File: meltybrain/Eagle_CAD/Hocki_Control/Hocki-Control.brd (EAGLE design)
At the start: 90 x 46 mm, 150 parts, among them J1 SM03B-SRSS-TB(LF)(SN), J2 SM03B-SRSS-TB(LF)(SN), J3 SM03B-SRSS-TB(LF)(SN), J4 SM04B-SRSS-TB(LF)(SN), J5 SM04B-SRSS-TB(LF)(SN), J6 SM02B-SRSS-TB(LF)(SN), U1 TEENSY_4.1, U10 TLV3502AIDCNR, U11 NL27WZ32USG, U12 NL27WZ32USG, U13 HMC1052L-TR, U14 LMV358, U15 IRF7509, U16 TMUX1219DCKR, U17 LMV358, U18 LMV358, U19 AP2210K-3.3TRG1, U2 ADXL375, U20 AP2210K-5.0TRG1, U21 AP63200, U22 74AHC1G04GW,125, U23 LDL212PU50R, U3 ADXL375, U4 ADXL375, U5 ADXL375, U6 LMH6612MAX/NOPB, U7 LMH6612MAX/NOPB, U8 LMH6612MAX/NOPB, U9 LMH6612MAX/NOPB

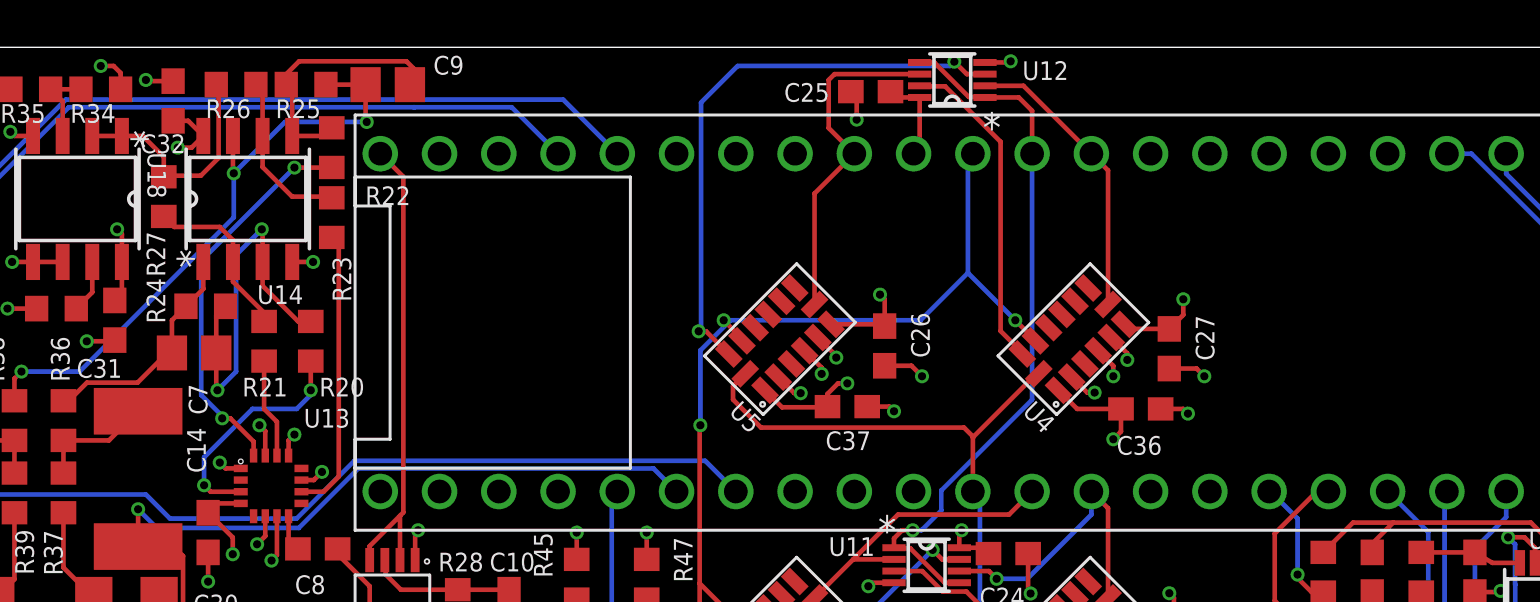
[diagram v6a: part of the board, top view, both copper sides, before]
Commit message: temperature sensor
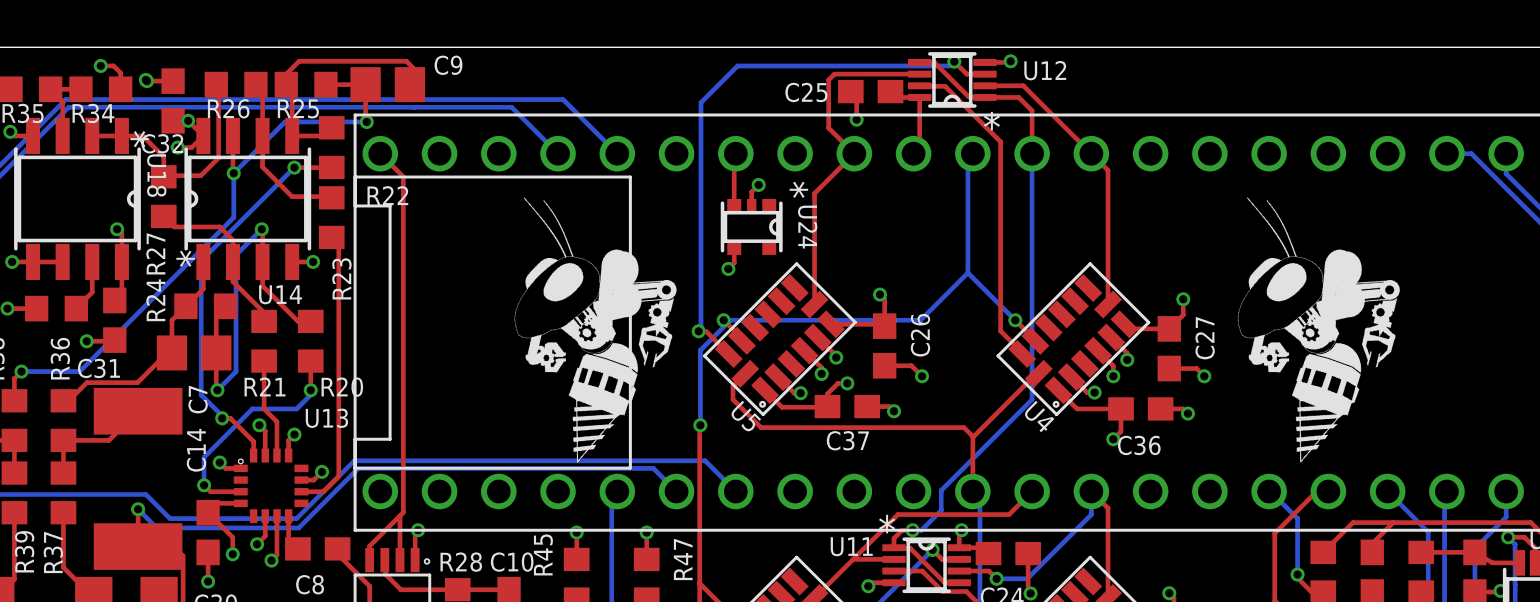
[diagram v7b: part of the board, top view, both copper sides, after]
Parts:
- added U$1, U$2: (no value), RoboJackets-Aesthetics:ROBOBUZZ_0.6X
- added U24: TMP235A4DCKR, Hocki_Library:SOT-353
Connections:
- new net TEMP: U1.26, U24.3
- net 3.3V: now also U24.4
- net GND: now also U24.2
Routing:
- net TEMP: track 0.00 -> 2.27 mm
- net GND: track 122.3 -> 123.3 mm, vias 100 -> 102
- net 3.3V: track 54.1 -> 55.1 mm, vias 13 -> 14
- net +3V3: vias 10 -> 11
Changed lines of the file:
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@@
 <drawing>
 <settings>
-<setting alwaysvectorfont="no"/>
+<setting alwaysvectorfont="yes"/>
 <setting verticaltext="up"/>
 </settings>
@@
 <layers>
 <layer number="1" name="Top" color="4" fill="1" visible="yes" active="yes"/>
-<layer number="2" name="GND" color="16" fill="1" visible="yes" active="yes"/>
+<layer number="2" name="GND" color="56" fill="1" visible="yes" active="yes"/>
 <layer number="3" name="Route3" color="17" fill="1" visible="no" active="no"/>
 <layer number="4" name="Route4" color="18" fill="1" visible="no" active="no"/>
@@
 <layer number="13" name="Route13" color="21" fill="1" visible="no" active="no"/>
 <layer number="14" name="Route14" color="22" fill="1" visible="no" active="no"/>
-<layer number="15" name="Power" color="23" fill="1" visible="yes" active="yes"/>
-<layer number="16" name="Bottom" color="1" fill="1" visible="yes" active="yes"/>
+<layer number="15" name="Power" color="22" fill="1" visible="yes" active="yes"/>
+<layer number="16" name="Bottom" color="9" fill="1" visible="yes" active="yes"/>
 <layer number="17" name="Pads" color="2" fill="1" visible="yes" active="yes"/>
 <layer number="18" name="Vias" color="2" fill="1" visible="yes" active="yes"/>
@@
 <attribute name="VALUE" x="23.6" y="1.8" size="1" layer="27" font="vector" align="top-left"/>
 </element>
+<element name="U$1" library="RoboJackets-Aesthetics" package="ROBOBUZZ_0.6X" value="" x="11" y="1" smashed="yes"/>
+<element name="U$2" library="RoboJackets-Aesthetics" package="ROBOBUZZ_0.6X" value="" x="-20" y="1" smashed="yes"/>
+<element name="U24" library="Hocki_Library" package="SOT-353" value="TMP235A4DCKR" x="-12.5" y="11.1" smashed="yes" rot="R270">
+<attribute name="NAME" x="-10.5" y="12.1" size="0.8" layer="25" font="vector" ratio="15" rot="SR270"/>
+<attribute name="VALUE" x="-14.5" y="12.1" size="1" layer="27" font="vector" rot="SR270" align="top-left"/>
+</element>
 </elements>
 <signals>
@@
 <wire x1="-25.4052" y1="-20" x2="-25" y2="-20.4052" width="0.2" layer="1"/>
 <via x="-25" y="-20.4052" extent="1-16" drill="0.35"/>
+<contactref element="U24" pad="2"/>
+<wire x1="-12.5" y1="12" x2="-12.5" y2="12.6" width="0.2" layer="1"/>
+<wire x1="-12.5" y1="12.6" x2="-12.2" y2="12.9" width="0.2" layer="1"/>
+<via x="-12.2" y="12.9" extent="1-16" drill="0.35"/>
+<via x="-38.4186" y="17.35" extent="1-16" drill="0.35"/>
 </signal>
 <signal name="3.3V">
@@
 <contactref element="D17" pad="C2"/>
 <wire x1="25.15" y1="2" x2="24.2" y2="2" width="0.2" layer="1"/>
+<contactref element="U24" pad="4"/>
+<wire x1="-13.25" y1="10.2" x2="-13.25" y2="9.55" width="0.2" layer="1"/>
+<wire x1="-13.25" y1="9.55" x2="-13.5" y2="9.3" width="0.2" layer="1"/>
+<via x="-13.5" y="9.3" extent="1-16" drill="0.35"/>
 </signal>
 <signal name="MOSI">
@@
 <wire x1="-31.5" y1="-9.2" x2="-31.5" y2="-8.3" width="0.2" layer="1"/>
 <wire x1="-31.5" y1="-8.3" x2="-31.2" y2="-8" width="0.2" layer="1"/>
+<via x="-36.655" y="15.65" extent="1-16" drill="0.35"/>
 </signal>
 <signal name="9V">
@@
 <wire x1="-51" y1="-17.15" x2="-51" y2="-15.85" width="0.2" layer="1"/>
 </signal>
+<signal name="TEMP">
+<contactref element="U24" pad="3"/>
+<contactref element="U1" pad="26"/>
+<wire x1="-13.25" y1="12" x2="-13.25" y2="14.17" width="0.2" layer="1"/>
+<wire x1="-13.25" y1="14.17" x2="-13.18" y2="14.24" width="0.2" layer="1"/>
+</signal>
 </signals>
 <mfgpreviewcolors>
-<mfgpreviewcolor name="soldermaskcolor" color="0xC8008000"/>
+<mfgpreviewcolor name="soldermaskcolor" color="0xC8000000"/>
 <mfgpreviewcolor name="silkscreencolor" color="0xFFFEFEFE"/>
 <mfgpreviewcolor name="backgroundcolor" color="0xFF282828"/>

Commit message: done
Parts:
- added C55: 1uF, rcl:C0603
- C1, C2, C3, C46: value 47nF -> 0.1uF; device rcl:C1206 -> rcl:C0603
- C11: value 1uF -> 2.2uF
- C13: value 47nF -> 2.2uF; device rcl:C1206 -> rcl:C0603
- C14: value 0.18uF -> 100pF; device Hocki_Library:ECH-U1H184GX9 -> rcl:C0603
- C15: value 47nF -> 100pF; device rcl:C1206 -> rcl:C0603
- C16: value 0.18uF -> 0.1u; device Hocki_Library:ECH-U1H184GX9 -> rcl:C0603
- C17: value 0.1uF -> 1uF
- C18: value 0.1uF -> 4.7uF
- C22, C23, C24, C25, C29, C31, C50: value 0.1uF -> 47nF; device rcl:C0603 -> rcl:C1206
- C30, C32: value 0.1uF -> 62nF; device rcl:C0603 -> Hocki_Library:BFC241646203
- C39, C41: value 1uF -> 0.1uF
- C4: value 47nF -> 10uF
- C40: value 2.2uF -> 0.1uF
- C42, C43, C49: value 100pF -> 0.1uF
- C44: value 2.2uF -> 1000pF; device rcl:C0603 -> rcl:C0805
- C45: value 47nF -> 0.18uF; device rcl:C1206 -> Hocki_Library:ECH-U1H184GX9
- C47: value 10uF -> 0.1uF; device rcl:C1206 -> rcl:C0603
- C48: value 22uF -> 47nF
- C5: value 62nF -> 100pF; device Hocki_Library:BFC241646203 -> rcl:C0603
- C51: value 0.1u -> 0.18uF; device rcl:C0603 -> Hocki_Library:ECH-U1H184GX9
- C52: value 22uF -> 1000pF; device rcl:C1206 -> rcl:C0805
- C53: value 4.7uF -> 0.1uF
- C54: value 1uF -> .1uF
- C6: value 62nF -> 22uF; device Hocki_Library:BFC241646203 -> rcl:C1206
- C7: value 1000pF -> 22uF; device rcl:C0805 -> rcl:C1206
- C8: value .1uF -> 1uF
- C9: value 1000pF -> 1uF; device rcl:C0805 -> rcl:C0603
- D1: value RB521S30T1G -> PESD4V0Y1BSFYL; device Hocki_Library:SOD-523 -> Hocki_Library:DSN0603-2
- D10, D9: value GREEN -> BAS581-02V-V-G-08; device SparkFun-LED:LED-0603 -> Hocki_Library:SOD-523
- D12: value GREEN -> PESD5V0H1BSFYL; device SparkFun-LED:LED-0603 -> Hocki_Library:DSN0603-2
- D13: value GREEN -> PESD4V0Y1BSFYL; device SparkFun-LED:LED-0603 -> Hocki_Library:DSN0603-2
- D14: value ESDZX051-1BF4 -> GREEN; device Hocki_Library:DSN0603-2 -> SparkFun-LED:LED-0603
- D15: value PESD5V0H1BSFYL -> BAS581-02V-V-G-08; device Hocki_Library:DSN0603-2 -> Hocki_Library:SOD-523
- D16, D17: value PESD4V0Y1BSFYL -> RB521S30T1G; device Hocki_Library:DSN0603-2 -> Hocki_Library:SOD-523
- D2: value RB521S30T1G -> BAS581-02V-V-G-08
- D3: value D26V0H1U2LP20-7 -> GREEN; device Hocki_Library:D26V0H1U2LP20-7 -> SparkFun-LED:LED-0603
- D4: value BAS581-02V-V-G-08 -> D26V0H1U2LP20-7; device Hocki_Library:SOD-523 -> Hocki_Library:D26V0H1U2LP20-7
- D5, D7: value BAS581-02V-V-G-08 -> GREEN; device Hocki_Library:SOD-523 -> SparkFun-LED:LED-0603
- D6: value BAS581-02V-V-G-08 -> ESDZX051-1BF4; device Hocki_Library:SOD-523 -> Hocki_Library:DSN0603-2
- J2: value SM03B-SRSS-TB(LF)(SN) -> SM04B-SRSS-TB(LF)(SN); device Hocki_Library:SM03B-SRSS-TB(LF)(SN) -> Hocki_Library:SM04B-SRSS-TB(LF)(SN)
- J3: value SM03B-SRSS-TB(LF)(SN) -> SM02B-SRSS-TB(LF)(SN); device Hocki_Library:SM03B-SRSS-TB(LF)(SN) -> Hocki_Library:SM02B-SRSS-TB(LF)(SN)
- J5: value SM04B-SRSS-TB(LF)(SN) -> SM03B-SRSS-TB(LF)(SN); device Hocki_Library:SM04B-SRSS-TB(LF)(SN) -> Hocki_Library:SM03B-SRSS-TB(LF)(SN)
- J6: value SM02B-SRSS-TB(LF)(SN) -> SM03B-SRSS-TB(LF)(SN); device Hocki_Library:SM02B-SRSS-TB(LF)(SN) -> Hocki_Library:SM03B-SRSS-TB(LF)(SN)
- R1: value 205k -> 665
- R10, R11: value 4.5k -> 169
- R13: value 169 -> 665
- R14, R45, R47: value 169 -> 499
- R15: value 20k -> 330
- R16: value 44.2k -> 4.5k
- R17: value 44.2k -> 169
- R18: value 30 -> 169
- R19: value 30 -> 4.5k
- R2: value 499 -> 665
- R20, R21, R31: value 4.99k -> 169
- R22, R32: value 4.99k -> 10k
- R23: value 4.99k -> 30
- R24: value 499k -> 44.2k
- R25: value 499k -> 30
- R26: value 499k -> 4.5k
- R27: value 499k -> 169
- R28: value 200 -> 169
- R29: value 665 -> 4.5k
- R3: value 169 -> 205k
- R30: value 330 -> 44.2k
- R33, R42: value 499 -> 499k
- R34: value 499 -> 40.2k
- R35: value 499 -> 7.32k
- R36, R38: value 40.2k -> 4.99k
- R37: value 7.32k -> 4.99k
- R39: value 7.32k -> 40.2k
- R4: value 4.5k -> 499
- R40: value 10k -> 7.32k
- R41: value 10k -> 4.99k
- R43: value 665 -> 499k
- R44: value 330 -> 499k
- R46: value 330 -> 200
- R48: value 665 -> 499
- R5: value 4.5k -> 20k
- R6, R8: value 169 -> 330
- R7, R9: value 169 -> 4.99k
- U1: value TEENSY_4.1 -> AP63200; device Hocki_Library:TEENSY_4.1 -> Hocki_Library:SOT-23-6
- U10: value TLV3502AIDCNR -> LMH6612MAX/NOPB; device Hocki_Library:SOT-23-8 -> Hocki_Library:8-SOIC
- U11: value NL27WZ32USG -> TLV3502AIDCNR; device Hocki_Library:US8 -> Hocki_Library:SOT-23-8
- U12: value NL27WZ32USG -> LMH6612MAX/NOPB; device Hocki_Library:US8 -> Hocki_Library:8-SOIC
- U13: value HMC1052L-TR -> TMP235A4DCKR; device Hocki_Library:16-LCC -> Hocki_Library:SOT-353
- U14, U17: value LMV358 -> ADXL375; device Hocki_Library:8-SOIC -> Hocki_Library:14-LGA
- U15: value IRF7509 -> NL27WZ32USG; device Hocki_Library:MICRO8 -> Hocki_Library:US8
- U16: value TMUX1219DCKR -> ADXL375; device Hocki_Library:SOT-363 -> Hocki_Library:14-LGA
- U18: value LMV358 -> NL27WZ32USG; device Hocki_Library:8-SOIC -> Hocki_Library:US8
- U19: value AP2210K-3.3TRG1 -> ADXL375; device Hocki_Library:SOT-23-5 -> Hocki_Library:14-LGA
- U2: value ADXL375 -> TEENSY_4.1; device Hocki_Library:14-LGA -> Hocki_Library:TEENSY_4.1
- U20: value AP2210K-5.0TRG1 -> LMV358; device Hocki_Library:SOT-23-5 -> Hocki_Library:8-SOIC
- U21: value AP63200 -> LMV358; device Hocki_Library:SOT-23-6 -> Hocki_Library:8-SOIC
- U22: value 74AHC1G04GW,125 -> HMC1052L-TR; device Hocki_Library:SOT-353 -> Hocki_Library:16-LCC
- U23: value LDL212PU50R -> LMV358; device Hocki_Library:DFN6(3X3) -> Hocki_Library:8-SOIC
- U24: value TMP235A4DCKR -> IRF7509; device Hocki_Library:SOT-353 -> Hocki_Library:MICRO8
- U3: value ADXL375 -> AP2210K-5.0TRG1; device Hocki_Library:14-LGA -> Hocki_Library:SOT-23-5
- U4: value ADXL375 -> AP2210K-3.3TRG1; device Hocki_Library:14-LGA -> Hocki_Library:SOT-23-5
- U5: value ADXL375 -> 74AHC1G04GW,125; device Hocki_Library:14-LGA -> Hocki_Library:SOT-353
- U6: value LMH6612MAX/NOPB -> LDL212PU50R; device Hocki_Library:8-SOIC -> Hocki_Library:DFN6(3X3)
- U9: value LMH6612MAX/NOPB -> TMUX1219DCKR; device Hocki_Library:8-SOIC -> Hocki_Library:SOT-363
- moved D8 85.5 mm to (36.1, -12.0), turned to 270 degrees
- moved U23 80.8 mm to (-41.7, 12.3)
- moved J3 80.1 mm to (-47.0, 10.0), turned to 270 degrees
- moved C53 77.0 mm to (-41.1, 7.60), flipped to the bottom
- moved C51 72.7 mm to (-48.4, 0.30)
- moved C16 71.7 mm to (23.5, 11.1)
- moved R40 70.1 mm to (-45.1, -0.30), turned to 90 degrees
- moved C32 69.8 mm to (26.5, -11.7), turned to 0 degrees
- moved C54 66.9 mm to (-31.1, -3.50), turned to 90 degrees
- moved C30 64.8 mm to (26.5, -19.9), turned to 0 degrees
- moved R24 64.2 mm to (21.4, -21.2), turned to 90 degrees
- moved D15 63.3 mm to (37.3, -15.2), turned to 90 degrees
- moved C5 63.0 mm to (-39.1, -13.1), turned to 180 degrees
- moved D12 62.4 mm to (-25.8, -20.0), turned to 180 degrees
- moved J2 61.6 mm to (33.0, 0.00), turned to 90 degrees
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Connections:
- net +24V: now also C4.1, D2.1, R1.2, U1.2, U1.3; no longer C47.1, D3.1, R48.2, U21.2, U21.3
- net +3V3: now also C13.1, C46.1, C47.1, C49.1, C53.1, D10.2, D13.C2, R10.2, R45.1, R46.1, U20.8, U21.8, U22.4, U23.8, U4.5; no longer C30.1, C31.1, C32.1, C33.1, C40.1, D16.C2, D6.2, R28.1, R34.1, R45.2, U13.4, U14.8, U17.8, U18.8, U19.5
- net +5V: now also C18.1, D15.2, J2.1, J2.S1, J2.S2, R8.2, U6.2, U6.3; no longer C53.1, D7.2, J5.1, J5.S1, J5.S2, R46.2, U23.2, U23.3
- net 1.66V_REF_BUF: now also C24.2, C25.2, C31.2, R19.1, R20.1, R29.1, R31.1, U8.6, U8.7; no longer C1.2, C3.2, C45.2, R10.1, R13.1, R4.1, R7.1, U6.6, U6.7
- net 1.6V_REF: now also R13.1, R15.2, U8.5; no longer R29.1, R30.2, U6.5
- net 10K_FB: now also C22.2, C23.2, R17.2; no longer C2.2, C46.2, R3.2
- net 10K_IN: now also C24.1, C25.1, R16.1, R17.1, R19.2; no longer C1.1, C45.1, R3.1, R4.2, R5.1
- net 10K_INT: now also R22.1, U11.7, U2.23; no longer R40.1, U1.23, U10.7
- net 10K_OUT: now also R12.2, R18.1, U12.3; no longer R6.2, R8.1, U9.3
- net 10K_PEAK: now also C30.1, D16.1, R23.2, R24.2, U12.2, U2.20; no longer C5.1, D1.1, R17.2, R18.2, U1.20, U9.2
- net 10K_REF: now also C8.1, R7.2, U11.2; no longer C12.1, R31.2, U10.2
- net 20K_FB: now also C29.2, R27.2, U10.7; no longer C4.2, R9.2, U8.7
- net 20K_IN: now also C31.1, R26.1, R27.1, R29.2, U10.3; no longer C3.1, R10.2, R11.1, R9.1, U8.3
- net 20K_INT: now also R32.1, U11.6, U2.22; no longer R41.1, U1.22, U10.6
- net 20K_OUT: now also R21.2, R28.1, U10.1, U12.5; no longer R12.2, R14.1, U8.1, U9.5
- net 20K_PEAK: now also C32.1, D17.1, R25.2, R30.2, U12.6, U2.21; no longer C6.1, D2.1, R16.2, R19.2, U1.21, U9.6
- net 20K_REF: now also C9.1, R9.2, U11.4; no longer C11.1, R32.2, U10.4
- net 3.3V: now also C1.1, C16.1, C33.1, C39.1, C40.1, C41.1, C42.1, C43.1, D1.C2, R11.2, U13.4, U14.1, U14.6, U15.8, U16.1, U16.6, U17.1, U17.6, U18.8, U19.1, U19.6, U2.3.3V1, U2.3.3V2, U5.5; no longer C22.1, C23.1, C24.1, C25.1, C26.1, C29.1, C51.1, D17.C2, R47.2, U1.3.3V1, U1.3.3V2, U10.8, U2.1, U2.6, U22.5, U24.4, U3.1, U3.6, U4.1, U4.6, U5.1, U5.6, U9.8
- net 5V: now also C11.1, C12.1, C2.1, C26.1, D10.1, D12.C2, D9.2, J1.2, J1.S1, J1.S2, R13.2, R6.2, U10.8, U2.5V, U3.5, U4.1, U4.3, U9.2; no longer C17.1, C18.1, C39.1, C44.1, D15.C2, D5.2, D6.1, J3.2, J3.S1, J3.S2, R29.2, R44.2, U1.5V, U16.2, U19.1, U19.3, U20.5, U6.8
- net 9V: now also C10.1, C17.1, C5.1, C6.1, C7.1, D15.1, D2.2, D6.C2, D9.1, J5.1, J6.1, R3.1, R4.2, U3.1, U3.3, U6.4, U6.6; no longer C41.1, C48.1, C49.1, C52.1, C54.1, D14.C2, D4.2, D5.1, D7.1, J1.1, J2.1, R1.1, R42.2, U20.1, U20.3, U23.4, U23.6
- net CS1: now also U14.7, U15.2, U2.14; no longer U1.14, U11.2, U2.7
- net CS2: now also U15.6, U16.7, U2.15; no longer U1.15, U11.6, U3.7
- net CS3: now also U17.7, U18.2, U2.10; no longer U1.10, U12.2, U4.7
- net CS4: now also U18.6, U19.7, U2.24; no longer U1.24, U12.6, U5.7
- net ESC_L: now also J3.1, U2.28; no longer J6.1, U1.28
- net ESC_R: now also J3.2, U2.29; no longer J6.2, U1.29
- net GND: now also C1.2, C14.2, C16.2, C2.2, C4.2, C46.2, C49.2, C50.2, C55.2, C7.2, C8.2, C9.2, D1.C1, D12.C1, D13.C1, D14.C, D3.C, D4.2, D5.C, D6.C1, D7.C, J2.4, J3.S1, J3.S2, J5.3, J5.S1, J5.S2, J6.3, R14.1, R15.1, R24.1, R47.2, R48.2, R5.2, U1.4, U10.4, U11.5, U13.2, U14.2, U14.5, U15.4, U16.2, U16.4, U16.5, U17.2, U17.5, U19.4, U19.5, U2.GND1, U2.GND2, U2.GND3, U20.4, U22.1, U22.11, U22.13, U22.15, U22.6, U22.7, U23.4, U23.5, U23.6, U24.1, U5.3, U6.1, U6.7, U9.3; no longer C22.2, C23.2, C24.2, C25.2, C29.2, C31.2, C44.2, C5.2, C51.2, C52.2, C54.2, D10.C, D12.C, D13.C, D14.C1, D15.C1, D16.C1, D17.C1, D3.2, D9.C, J1.S1, J1.S2, J2.3, J2.S1, J2.S2, J3.3, J5.4, R15.2, R16.1, R17.1, R2.1, R33.2, R35.2, U1.GND1, U1.GND2, U1.GND3, U10.5, U11.4, U13.1, U13.11, U13.13, U13.15, U13.6, U13.7, U15.1, U16.3, U18.5, U18.6, U2.2, U2.4, U2.5, U20.2, U22.3, U23.1, U23.7, U24.2, U3.4, U3.5, U4.4, U4.5, U5.2, U5.4, U5.5, U6.4, U9.4
- net IR_BOTTOM: now also J6.2, U9.6; no longer J2.2, U16.6
- net IR_SEL: now also U2.37, U9.1; no longer U1.37, U16.1
- net IR_TOP: now also J5.2, U9.4; no longer J1.2, U16.4
- net LED_CLK1: now also J2.2, U2.2; no longer J4.2, U1.2
- net LED_CLK2: now also J4.2, U2.4; no longer J5.2, U1.4
- net LED_DATA1: now also J2.3, U2.1; no longer J4.3, U1.1
- net LED_DATA2: now also J4.3, U2.3; no longer J5.3, U1.3
- net MAG_FILT_A: now also C45.2, U2.38, U21.1, U21.2; no longer C14.2, U1.38, U17.1, U17.2
- net MAG_FILT_B: now also C51.2, U2.39, U21.6, U21.7; no longer C16.2, U1.39, U17.6, U17.7
- net MAG_OUTPUTA: now also C44.2, R33.1, R34.2, U20.1; no longer C7.2, R24.1, R36.2, U14.1
- net MAG_OUTPUTB: now also C52.2, R39.2, R44.1, U20.7; no longer C9.2, R25.1, R38.2, U14.7
- net MISO: now also U14.12, U16.12, U17.12, U19.12; no longer U1.12, U3.12, U4.12, U5.12
- net MOSI: now also U15.1, U15.5, U18.1, U18.5, U2.11; no longer U1.11, U11.1, U11.5, U12.1, U12.5
- net MOSI1: now also U14.13, U15.7; no longer U11.7, U2.13
- net MOSI2: now also U15.3, U16.13; no longer U11.3, U3.13
- net MOSI3: now also U17.13, U18.7; no longer U12.7, U4.13
- net MOSI4: now also U18.3, U19.13; no longer U12.3, U5.13
- net N$1: now also C3.1, U1.6; no longer C50.1, U21.6
- net N$10: now also C29.1, R21.1, U10.2, U10.6; no longer C4.1, R12.1, U8.2, U8.6
- net N$11: now also C15.1, U4.4; no longer C43.1, U19.4
- net N$12: now also C5.2, R3.2, R5.1, U1.1; no longer C49.2, R1.2, R15.1, U21.1
- net N$13: now also R28.2, R31.2, U10.5; no longer R13.2, R14.2, U8.5
- net N$14: now also D8.A, R8.1; no longer D12.A, R46.1
- net N$15: now also D7.A, R6.1; no longer D10.A, R44.1
- net N$16: now also C54.1, U24.5, U24.6, U24.7, U24.8; no longer C8.1, U15.5, U15.6, U15.7, U15.8
- net N$17: now also R10.1; no longer R45.1
- net N$18: now also D5.A, R4.1; no longer D9.A, R42.1
- net N$19: now also D3.A, R2.1; no longer D8.A, R43.1
- net N$2: now also D16.2, U12.1; no longer D1.2, U9.1
- net N$20: now also R1.1, R2.2; no longer R43.2, R48.1
- net N$21: now also R7.1, U2.18; no longer R31.1, U1.18
- net N$22: now also R9.1, U2.19; no longer R32.1, U1.19
- net N$23: now also R45.2, R47.1, U23.3; no longer R34.2, R35.1, U18.3
- net N$24: now also R48.1, U23.7; no longer R33.1, U18.7
- net N$25: now also C45.1, R34.1, R35.2; no longer C14.1, R36.1, R37.2
- net N$26: now also C48.1, R35.1, U21.3; no longer C13.1, R37.1, U17.3
- net N$27: now also D14.A, R11.1; no longer D13.A, R47.1
- net N$29: now also C51.1, R39.1, R40.2; no longer C16.1, R38.1, R39.2
- net N$3: now also C3.2, U1.5; no longer C50.2, U21.5
- net N$30: now also C50.1, R40.1, U21.5; no longer C15.1, R39.1, U17.5
- net N$34: now also R41.1, R43.1, U20.6; no longer R23.1, R26.1, U14.6
- net N$35: now also C52.1, R38.1, R44.2, U20.5; no longer C9.1, R22.1, R25.2, U14.5
- net N$36: now also R37.1, R42.1, U20.2; no longer R21.1, R27.1, U14.2
- net N$37: now also C44.1, R33.2, R36.1, U20.3; no longer C7.1, R20.1, R24.2, U14.3
- net N$4: now also C22.1, C23.1, R12.1; no longer C2.1, C46.1, R6.1
- net N$5: now also R22.2, R23.1, U11.1; no longer R18.1, R40.2, U10.1
- net N$6: now also R25.1, R32.2, U11.3; no longer R19.1, R41.2, U10.3
- net N$7: now also R18.2, R20.2; no longer R7.2, R8.2
- net N$8: now also C14.1, U3.4; no longer C42.1, U20.4
- net N$9: now also D17.2, U12.7; no longer D2.2, U9.7
- net OUT+(A): now also R36.2, U22.3; no longer R20.2, U13.3
- net OUT+(B): now also R38.2, U22.16; no longer R22.2, U13.16
- net OUT-(A): now also R37.2, U22.14; no longer R21.2, U13.14
- net OUT-(B): now also R41.2, U22.10; no longer R23.2, U13.10
- net RC_SIGNAL: now also J1.1, U5.2; no longer J3.1, U22.2
- net S/R: now also U2.32, U24.2, U24.4; no longer U1.32, U15.2, U15.4
- net S/R+: now also C54.2, U22.8; no longer C8.2, U13.8
- net SBUS: now also U2.0, U5.4; no longer U1.0, U22.4
- net SCLK: now also U14.14, U16.14, U17.14, U19.14, U2.13; no longer U1.13, U2.14, U3.14, U4.14, U5.14
- net TEMP: now also U13.3, U2.26; no longer U1.26, U24.3
- net VG_SIGNAL: now also R14.2, U8.3, U9.5; no longer R2.2, U16.5, U6.3
- net VG_SIGNAL_BUF: now also R16.2, R26.2, U8.1, U8.2; no longer R11.2, R5.2, U6.1, U6.2
- net VREF/2: now also R42.2, R43.2, U23.1, U23.2; no longer R26.2, R27.2, U18.1, U18.2
- net VSR: now also C55.1, R46.2, U24.3; no longer C10.1, R28.2, U15.3
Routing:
- net N$24: track 2.28 -> 7.14 mm, vias 0 -> 1
- net 1.6V_REF: track 15.1 -> 10.4 mm, vias 0 -> 1
- net N$4: track 19.4 -> 14.8 mm
- net 3.3V: track 55.1 -> 50.4 mm, vias 14 -> 15
- net N$23: track 3.51 -> 6.22 mm, vias 0 -> 1
- net GND: track 123.3 -> 120.7 mm, vias 102 -> 101
- net 9V: track 114.7 -> 112.1 mm, vias 6 -> 8
- net N$8: track 3.93 -> 1.51 mm
- net 10K_PEAK: track 50.5 -> 52.8 mm
- net CS4: track 14.8 -> 13.1 mm
- net MAG_FILT_B: track 48.0 -> 49.4 mm
- net MAG_FILT_A: track 38.4 -> 39.8 mm
- net N$20: track 1.30 -> 2.68 mm
- net N$22: track 14.3 -> 13.0 mm
- net 10K_REF: track 13.1 -> 14.2 mm
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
